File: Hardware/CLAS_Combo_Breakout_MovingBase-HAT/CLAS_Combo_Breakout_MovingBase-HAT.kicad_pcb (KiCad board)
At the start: 4 copper layers, 38.5 x 60 mm, 10 parts, among them J2 ZED, J3 NEO

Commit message: カイロズカッコカリ
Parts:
- added REF**: Converter_DCDC_AnalogDevices_LTM4693, Converter_DCDC_extlib:Converter_DCDC_AnalogDevices_LTM4693, F.Cu at (136.9, 100.7)
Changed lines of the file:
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@@
   (net 15 "/EXTINT_NEO")
   (net 16 "/RXD1_NEO")
+  (footprint "Converter_DCDC_extlib:Converter_DCDC_AnalogDevices_LTM4693" (layer "F.Cu")
+    (at 136.858 100.696)
+    (tags "LTM4693")
+    (attr smd)
+    (fp_text reference "REF**" (at 0 -3.175 unlocked) (layer "F.SilkS")
+      (effects (font (size 1 1) (thickness 0.15)))
+    )
+    (fp_text value "Converter_DCDC_AnalogDevices_LTM4693" (at 0 3.175 unlocked) (layer "F.Fab")
+      (effects (font (size 1 1) (thickness 0.15)))
+    )
+    (fp_text user "${REFERENCE}" (at 0 -3.175 unlocked) (layer "F.Fab")
+      (effects (font (size 1 1) (thickness 0.15)))
+    )
+    (fp_line (start 1.8796 -2.1209) (end -1.8796 -2.1209) (layer "F.SilkS") (width 0.12))
+    (fp_line (start 1.8796 2.1209) (end 1.8796 -2.1209) (layer "F.SilkS") (width 0.12))
+    (fp_line (start -1.3 -2.3609) (end -2.1196 -2.3609) (layer "F.SilkS") (width 0.12))
+    (fp_line (start -2.1196 -2.3609) (end -2.1196 -1.3) (layer "F.SilkS") (width 0.12))
+    (fp_line (start -1.8796 2.1209) (end 1.8796 2.1209) (layer "F.SilkS") (width 0.12))
+    (fp_line (start -1.8796 -2.1209) (end -1.8796 2.1209) (layer "F.SilkS") (width 0.12))
+    (fp_line (start 2.0066 -2.2479) (end 2.0066 2.2479) (layer "F.CrtYd") (width 0.05))
+    (fp_line (start -2.0066 -2.2479) (end 2.0066 -2.2479) (layer "F.CrtYd") (width 0.05))
+    (fp_line (start 2.0066 2.2479) (end -2.0066 2.2479) (layer "F.CrtYd") (width 0.05))
+    (fp_line (start -2.0066 2.2479) (end -2.0066 -2.2479) (layer "F.CrtYd") (width 0.05))
+    (fp_line (start 1.7526 -1.9939) (end -1.7526 -1.9939) (layer "F.Fab") (width 0.1))
+    (fp_line (start -1.4276 -1.9939) (end -1.7526 -1.6689) (layer "F.Fab") (width 0.1))
+    (fp_line (start 1.7526 1.9939) (end 1.7526 -1.9939) (layer "F.Fab") (width 0.1))
+    (fp_line (start -1.7526 1.9939) (end 1.7526 1.9939) (layer "F.Fab") (width 0.1))
+    (fp_line (start -1.7526 -1.9939) (end -1.7526 1.9939) (layer "F.Fab") (width 0.1))
+    (pad "A1" smd circle (at -1.3 -1.3) (size 0.45 0.45) (layers "F.Cu" "F.Paste" "F.Mask")
+      (solder_mask_margin -0.05) (solder_paste_margin -0.05))
+    (pad "A2" smd circle (at -0.65 -1.3) (size 0.45 0.45) (layers "F.Cu" "F.Paste" "F.Mask")
+      (solder_mask_margin -0.05) (solder_paste_margin -0.05))
+    (pad "A3" smd circle (at 0 -1.3) (size 0.45 0.45) (layers "F.Cu" "F.Paste" "F.Mask")
+      (solder_mask_margin -0.05) (solder_paste_margin -0.05))
+    (pad "A4" smd circle (at 0.65 -1.3) (size 0.45 0.45) (layers "F.Cu" "F.Paste" "F.Mask")
+      (solder_mask_margin -0.05) (solder_paste_margin -0.05))
+    (pad "A5" smd circle (at 1.3 -1.3) (size 0.45 0.45) (layers "F.Cu" "F.Paste" "F.Mask")
+      (solder_mask_margin -0.05) (solder_paste_margin -0.05))
+    (pad "B1" smd circle (at -1.3 -0.65) (size 0.45 0.45) (layers "F.Cu" "F.Paste" "F.Mask")
+      (solder_mask_margin -0.05) (solder_paste_margin -0.05))
+    (pad "B2" smd circle (at -0.65 -0.65) (size 0.45 0.45) (layers "F.Cu" "F.Paste" "F.Mask")
+      (solder_mask_margin -0.05) (solder_paste_margin -0.05))
+    (pad "B3" smd circle (at 0 -0.65) (size 0.45 0.45) (layers "F.Cu" "F.Paste" "F.Mask")
+      (solder_mask_margin -0.05) (solder_paste_margin -0.05))
+    (pad "B4" smd circle (at 0.65 -0.65) (size 0.45 0.45) (layers "F.Cu" "F.Paste" "F.Mask")
+      (solder_mask_margin -0.05) (solder_paste_margin -0.05))
+    (pad "B5" smd circle (at 1.3 -0.65) (size 0.45 0.45) (layers "F.Cu" "F.Paste" "F.Mask")
+      (solder_mask_margin -0.05) (solder_paste_margin -0.05))
+    (pad "C1" smd circle (at -1.3 0) (size 0.45 0.45) (layers "F.Cu" "F.Paste" "F.Mask")
+      (solder_mask_margin -0.05) (solder_paste_margin -0.05))
+    (pad "C2" smd circle (at -0.65 0) (size 0.45 0.45) (layers "F.Cu" "F.Paste" "F.Mask")
+      (solder_mask_margin -0.05) (solder_paste_margin -0.05))
+    (pad "C3" smd circle (at 0 0) (size 0.45 0.45) (layers "F.Cu" "F.Paste" "F.Mask")
+      (solder_mask_margin -0.05) (solder_paste_margin -0.05))
+    (pad "C4" smd circle (at 0.65 0) (size 0.45 0.45) (layers "F.Cu" "F.Paste" "F.Mask")
+      (solder_mask_margin -0.05) (solder_paste_margin -0.05))
+    (pad "C5" smd circle (at 1.3 0) (size 0.45 0.45) (layers "F.Cu" "F.Paste" "F.Mask")
+      (solder_mask_margin -0.05) (solder_paste_margin -0.05))
+    (pad "D1" smd circle (at -1.3 0.65) (size 0.45 0.45) (layers "F.Cu" "F.Paste" "F.Mask")
+      (solder_mask_margin -0.05) (solder_paste_margin -0.05))
+    (pad "D2" smd circle (at -0.65 0.65) (size 0.45 0.45) (layers "F.Cu" "F.Paste" "F.Mask")
+      (solder_mask_margin -0.05) (solder_paste_margin -0.05))
+    (pad "D3" smd circle (at 0 0.65) (size 0.45 0.45) (layers "F.Cu" "F.Paste" "F.Mask")
+      (solder_mask_margin -0.05) (solder_paste_margin -0.05))
+    (pad "D4" smd circle (at 0.65 0.65) (size 0.45 0.45) (layers "F.Cu" "F.Paste" "F.Mask")
+      (solder_mask_margin -0.05) (solder_paste_margin -0.05))
+    (pad "D5" smd circle (at 1.3 0.65) (size 0.45 0.45) (layers "F.Cu" "F.Paste" "F.Mask")
+      (solder_mask_margin -0.05) (solder_paste_margin -0.05))
+    (pad "E1" smd circle (at -1.3 1.3) (size 0.45 0.45) (layers "F.Cu" "F.Paste" "F.Mask")
+      (solder_mask_margin -0.05) (solder_paste_margin -0.05))
+    (pad "E2" smd circle (at -0.65 1.3) (size 0.45 0.45) (layers "F.Cu" "F.Paste" "F.Mask")
+      (solder_mask_margin -0.05) (solder_paste_margin -0.05))
+    (pad "E3" smd circle (at 0 1.3) (size 0.45 0.45) (layers "F.Cu" "F.Paste" "F.Mask")
+      (solder_mask_margin -0.05) (solder_paste_margin -0.05))
+    (pad "E4" smd circle (at 0.65 1.3) (size 0.45 0.45) (layers "F.Cu" "F.Paste" "F.Mask")
+      (solder_mask_margin -0.05) (solder_paste_margin -0.05))
+    (pad "E5" smd circle (at 1.3 1.3) (size 0.45 0.45) (layers "F.Cu" "F.Paste" "F.Mask")
+      (solder_mask_margin -0.05) (solder_paste_margin -0.05))
+    (model "${KIPRJMOD}/../../ExternalLib/Converter_DCDC_extlib/LTM4693.stp"
+      (offset (xyz 0 0 0))
+      (scale (xyz 1 1 1))
+      (rotate (xyz 0 0 0))
+    )
+  )
   (footprint "Connector_PinHeader_2.54mm:PinHeader_1x11_P2.54mm_Vertical" locked (layer "F.Cu")
     (at 127.94 147.912 90)

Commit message: 配線４割
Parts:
- removed the REF** at (136.9, 100.7)
- removed the REF** at (159.0, 96.0)
- removed the REF** at (160.0, 140.0)
- added C1: 0.1u, Capacitor_SMD:C_0603_1608Metric, F.Cu at (138.1, 122.0)
- added C10: 100μF10V X5R 3216, Capacitor_SMD:C_1206_3216Metric, F.Cu at (146.8, 138.8)
- added C11: 2200pF50V CH 1608, Capacitor_SMD:C_0603_1608Metric, F.Cu at (142.7, 145.4)
- added C12: 220μF4V X6S 3216, Capacitor_SMD:C_1206_3216Metric, F.Cu at (146.8, 144.9)
- added C2: 0.1u, Capacitor_SMD:C_0603_1608Metric, F.Cu at (133.0, 126.1)
- added C3: 0.1u, Capacitor_SMD:C_0603_1608Metric, F.Cu at (138.6, 156.6)
- added C4: 1u, Capacitor_SMD:C_0603_1608Metric, F.Cu at (140.7, 127.1)
- added C5: 0.1u, Capacitor_SMD:C_0603_1608Metric, F.Cu at (140.7, 125.6)
- added C6: 0.1u, Capacitor_SMD:C_0603_1608Metric, F.Cu at (138.1, 119.0)
- added C7: 47μF6.3V X5R 1608, Capacitor_SMD:C_0603_1608Metric, F.Cu at (143.2, 114.4)
- added C8: 0.1u, Capacitor_SMD:C_0603_1608Metric, F.Cu at (148.3, 132.7)
- added C9: 47μF6.3V X5R 1608, Capacitor_SMD:C_0603_1608Metric, F.Cu at (142.2, 132.7)
- added D1: CUHS20S30, CUHS20S30:CUHS20S30, F.Cu at (141.2, 118.0)
- added D2: RED, LED_SMD:LED_0603_1608Metric, F.Cu at (148.3, 129.7)
- added D3: GREEN, LED_SMD:LED_0603_1608Metric, F.Cu at (142.2, 129.7)
- added D4: RTK, LED_SMD:LED_0603_1608Metric, F.Cu at (130.5, 154.5)
- added D5: GEO, LED_SMD:LED_0603_1608Metric, F.Cu at (130.5, 157.1)
- added D6: PPS, LED_SMD:LED_0603_1608Metric, F.Cu at (130.5, 159.6)
- added D7: CUHS20S30, CUHS20S30:CUHS20S30, F.Cu at (145.2, 135.7)
- added J2: SMA, Connector_Coaxial_extlib:SMA_Molex_0732512440_embed, B.Cu at (148.5, 97.5)
- added J3: SWD, Connector_PinHeader_1.27mm:PinHeader_2x05_P1.27mm_Vertical, F.Cu at (138.1, 104.3)
- added J5: BATT, Connector_JST:JST_PH_S2B-PH-SM4-TB_1x02-1MP_P2.00mm_Horizontal, F.Cu at (136.3, 134.2)
- added J7: USB_C_Receptacle_USB2.0, Connector_USB_extlib:USB_C_Receptacle_5077CR-16-SMC2-BK-TR, F.Cu at (144.7, 108.3)
- added Q1: AO3415A, Package_TO_SOT_SMD:SOT-23, F.Cu at (142.7, 136.3)
- added R1: 33, Resistor_SMD:R_0603_1608Metric, F.Cu at (141.2, 122.0)
- added R10: 1M, Resistor_SMD:R_0603_1608Metric, F.Cu at (140.7, 130.9)
- added R11: 510k, Resistor_SMD:R_0603_1608Metric, F.Cu at (139.9, 128.6)
- added R12: 100k, Resistor_SMD:R_0603_1608Metric, F.Cu at (148.3, 135.7)
- added R13: 10, Resistor_SMD:R_0603_1608Metric, F.Cu at (146.8, 135.7)
- added R14: Rtop, Resistor_SMD:R_0603_1608Metric, F.Cu at (142.7, 139.3)
- added R15: Rbtm, Resistor_SMD:R_0603_1608Metric, F.Cu at (142.7, 140.8)
- added R16: 5.1k, Resistor_SMD:R_0603_1608Metric, F.Cu at (146.3, 102.7)
- added R17: 5.1k, Resistor_SMD:R_0603_1608Metric, F.Cu at (143.2, 102.7)
- added R18: 10k, Resistor_SMD:R_0603_1608Metric, F.Cu at (142.7, 143.9)
- added R19: 26.2k, Resistor_SMD:R_0603_1608Metric, F.Cu at (142.7, 142.4)
- added R2: 33, Resistor_SMD:R_0603_1608Metric, F.Cu at (134.6, 126.1)
- added R3: 10k, Resistor_SMD:R_0603_1608Metric, F.Cu at (139.7, 119.0)
- added R4: RILIM, Resistor_SMD:R_0603_1608Metric, F.Cu at (145.2, 129.7)
- added R5: 1k, Resistor_SMD:R_0603_1608Metric, F.Cu at (146.8, 129.7)
- added R6: 1k, Resistor_SMD:R_0603_1608Metric, F.Cu at (143.7, 129.7)
- added R7: 1k, Resistor_SMD:R_0603_1608Metric, F.Cu at (134.1, 154.5)
- added R8: 1k, Resistor_SMD:R_0603_1608Metric, F.Cu at (134.1, 157.1)
- added R9: 1k, Resistor_SMD:R_0603_1608Metric, F.Cu at (134.1, 159.6)
- added REF**: LiPo_3.7V_500mAh_503030, Battery_extlib:LiPo_3.7V_500mAh_503030, B.Cu at (145.0, 130.0)
- added SW1: SW_Push, Button_Switch_SMD:SW_Push_1P1T_NO_Vertical_Wuerth_434133025816, F.Cu at (134.6, 115.9)
- added SW2: SW_SPDT, Button_Switch_SMD_extlib:SW_SPDT_SSSS213202, F.Cu at (136.6, 142.4)
- added U1: CH340K, Package_SO:SSOP-10_3.9x4.9mm_P1.00mm, F.Cu at (134.6, 121.0)
- added U2: TMUX136, Package_DFN_QFN:Texas_R-PUQFN-N10, F.Cu at (136.6, 126.1)
- added U3: ISP4520-AS, RF_Module_extlib:ISP4520-AS_with_Keep-Out, F.Cu at (159.5, 115.5)
- added U4: MCP73831-2-OT, Package_TO_SOT_SMD:SOT-23-5, F.Cu at (145.2, 132.7)
- added U5: LTM4693, Converter_DCDC_extlib:Converter_DCDC_AnalogDevices_LTM4693, F.Cu at (146.8, 141.8)
- added U6: USBLC6-2P6, Package_TO_SOT_SMD:SOT-666, F.Cu at (139.7, 112.9)
- J1: renamed from J**; value 0734152063 -> MMCX
- moved H4 66.9 mm to (144.0, 158.0)
- renumbered J2 to J4, J3 to J6
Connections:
- J1 pad 1: (no net) -> Net-(J1-Pad1)
- J1 pad 2: (no net) -> GND
- J6 pad 2: /RESET -> /RESET_ZED_NEO
- J6 pad 8: /SDA -> unconnected-(J6-Pad8)
- J6 pad 9: /SCL -> unconnected-(J6-Pad9)
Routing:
- net Net-(R15-Pad1): track 0.00 -> 15.8 mm
- net VBUS: track 0.00 -> 10.5 mm
- net +BATT: track 0.00 -> 9.61 mm
- net VDD: track 0.00 -> 8.55 mm
- net Net-(Q1-Pad1): track 0.00 -> 7.82 mm, vias 0 -> 2
- net Net-(R14-Pad2): track 0.00 -> 7.52 mm
- net /~{CHG_STAT}: track 0.00 -> 5.39 mm
- net +3.3V: track 0.00 -> 3.39 mm
- net Net-(R18-Pad1): track 0.00 -> 2.24 mm
- net Net-(R4-Pad2): track 0.00 -> 2.20 mm
- net Net-(R19-Pad1): track 0.00 -> 2.00 mm
- net Net-(C11-Pad1): track 0.00 -> 1.54 mm
- net Net-(D3-Pad2): track 0.00 -> 1.54 mm
- net Net-(D2-Pad1): track 0.00 -> 1.54 mm
- net /VBAT: track 0.00 -> 1.49 mm
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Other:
- outline, holes or cut-outs redrawn
- board text added: "CHG"
- board text added: "FULL"
- board text added: "ISP4520のy位置はkeep-outエリアの下側が 右下MHのすぐ上にくるように配置"
- board text added: "PROG"
- board text added: "SMAコネクタのサーマルリリーフ消す"
- board text added: "SMAコネクタは下のボードのUSBコネクタに干渉しない位置 なおType-Cケーブルを接続する場合については未確認"
- board text added: "左側の基板エッジは左上のMHに従属"

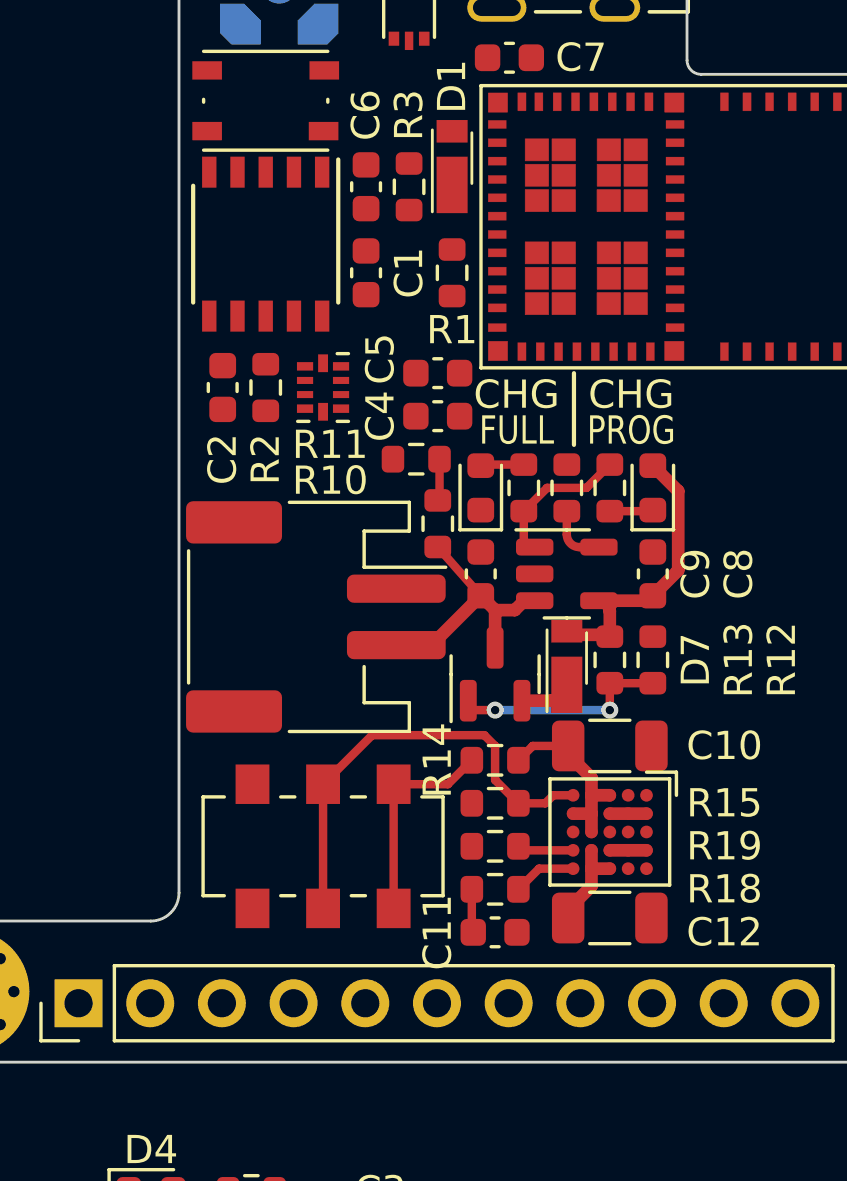
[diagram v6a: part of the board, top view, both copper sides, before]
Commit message: ISP4520の公式のフットプリントの間違いを修正
メーカーが提供しているフットプリントでも信用しないようにしましょう
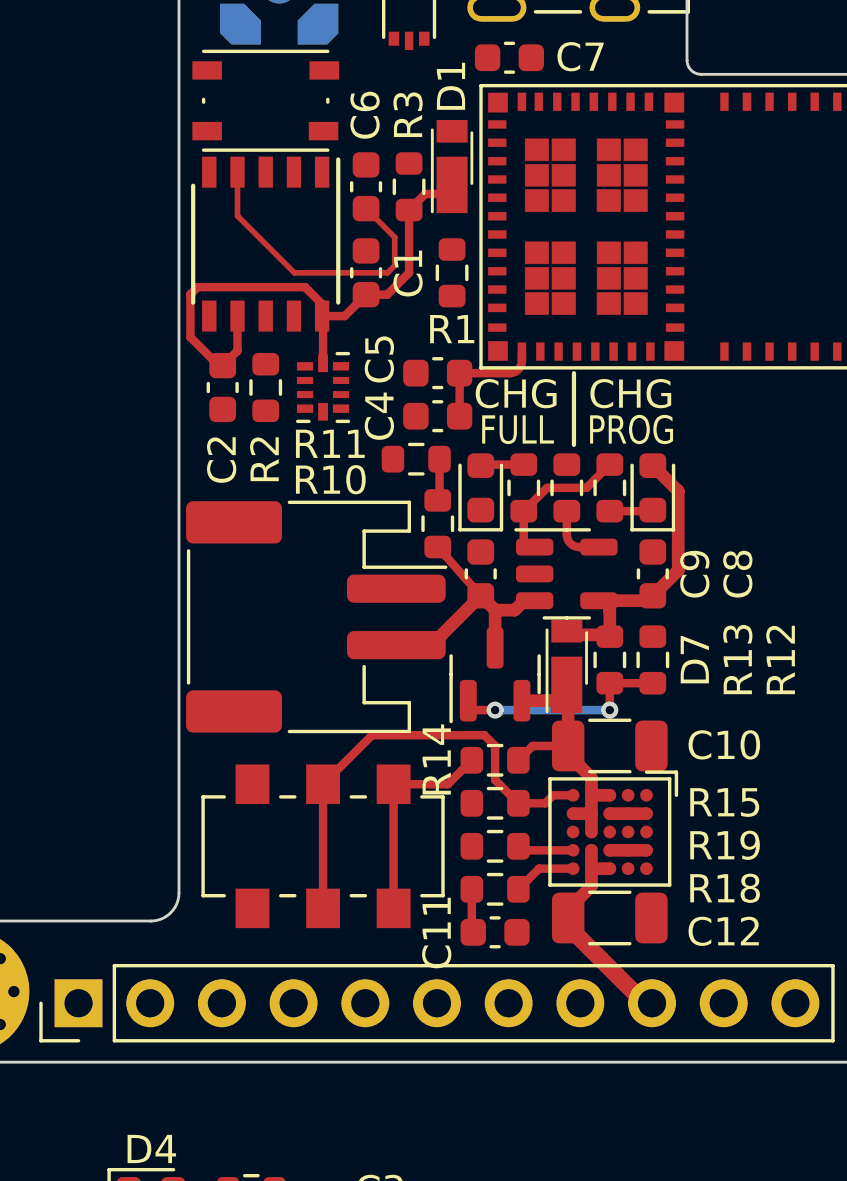
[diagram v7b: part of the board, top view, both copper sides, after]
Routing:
- net +3.3V: track 3.39 -> 32.3 mm
- net /DTR: track 0.00 -> 10.5 mm
- net VDD: track 8.55 -> 10.7 mm
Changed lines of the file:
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@@
     (effects (font (size 1 1) (thickness 0.15)) (justify left))
   )
+  (segment (start 141.443 125.588) (end 141.443 127.112) (width 0.3) (layer "F.Cu") (net 2))
+  (segment (start 137.369 123.566) (end 138.128 122.807) (width 0.3) (layer "F.Cu") (net 2))
+  (segment (start 138.877 122.807) (end 138.128 122.807) (width 0.3) (layer "F.Cu") (net 2))
+  (segment (start 131.905 124.318) (end 131.905 122.794) (width 0.3) (layer "F.Cu") (net 2))
   (segment (start 146.114 142.494) (end 146.114 143.144) (width 0.45) (layer "F.Cu") (net 2))
+  (segment (start 132.908 125.321) (end 131.905 124.318) (width 0.3) (layer "F.Cu") (net 2))
+  (segment (start 139.652 119.809) (end 139.652 122.032) (width 0.3) (layer "F.Cu") (net 2))
+  (segment (start 132.159 122.54) (end 135.969 122.54) (width 0.3) (layer "F.Cu") (net 2))
+  (segment (start 141.176 118.918) (end 141.176 119.238) (width 0.3) (layer "F.Cu") (net 2))
   (segment (start 145.289 144.589) (end 145.289 144.892) (width 0.45) (layer "F.Cu") (net 2))
+  (segment (start 145.289 144.892) (end 145.289 145.195) (width 0.6) (layer "F.Cu") (net 2))
+  (segment (start 136.572 123.566) (end 137.369 123.566) (width 0.3) (layer "F.Cu") (net 2))
+  (segment (start 139.652 122.032) (end 138.877 122.807) (width 0.3) (layer "F.Cu") (net 2))
+  (segment (start 131.905 122.794) (end 132.159 122.54) (width 0.3) (layer "F.Cu") (net 2))
+  (segment (start 135.969 122.54) (end 136.572 123.143) (width 0.3) (layer "F.Cu") (net 2))
+  (segment (start 133.572 124.797) (end 133.048 125.321) (width 0.3) (layer "F.Cu") (net 2))
   (segment (start 146.114 143.764) (end 145.289 144.589) (width 0.45) (layer "F.Cu") (net 2))
+  (segment (start 133.048 125.321) (end 132.908 125.321) (width 0.3) (layer "F.Cu") (net 2))
+  (segment (start 148.006 147.912) (end 148.26 147.912) (width 0.6) (layer "F.Cu") (net 2))
+  (segment (start 145.289 145.195) (end 148.006 147.912) (width 0.6) (layer "F.Cu") (net 2))
+  (segment (start 143.65 124.825) (end 143.65 125.146) (width 0.3) (layer "F.Cu") (net 2))
+  (segment (start 136.572 123.143) (end 136.572 123.566) (width 0.3) (layer "F.Cu") (net 2))
+  (segment (start 141.176 119.238) (end 140.223 119.238) (width 0.3) (layer "F.Cu") (net 2))
+  (segment (start 133.572 123.566) (end 133.572 124.797) (width 0.3) (layer "F.Cu") (net 2))
   (segment (start 146.114 143.144) (end 146.114 143.764) (width 0.45) (layer "F.Cu") (net 2))
+  (segment (start 136.604 123.598) (end 136.572 123.566) (width 0.3) (layer "F.Cu") (net 2))
   (segment (start 146.114 143.144) (end 146.764 143.144) (width 0.45) (layer "F.Cu") (net 2))
+  (segment (start 140.223 119.238) (end 139.652 119.809) (width 0.3) (layer "F.Cu") (net 2))
+  (segment (start 136.604 125.236) (end 136.604 123.598) (width 0.3) (layer "F.Cu") (net 2))
+  (segment (start 143.208 125.588) (end 141.443 125.588) (width 0.3) (layer "F.Cu") (net 2))
+  (arc (start 143.65 125.146) (mid 143.520541 125.458541) (end 143.208 125.588) (width 0.3) (layer "F.Cu") (net 2))
+  (segment (start 139.144 121.778) (end 138.89 122.032) (width 0.2) (layer "F.Cu") (net 17))
+  (segment (start 139.144 120.775) (end 139.144 121.778) (width 0.2) (layer "F.Cu") (net 17))
+  (segment (start 138.128 119.759) (end 139.144 120.775) (width 0.2) (layer "F.Cu") (net 17))
+  (segment (start 135.588 122.032) (end 133.572 120.016) (width 0.2) (layer "F.Cu") (net 17))
+  (segment (start 133.572 120.016) (end 133.572 118.466) (width 0.2) (layer "F.Cu") (net 17))
+  (segment (start 138.89 122.032) (end 135.588 122.032) (width 0.2) (layer "F.Cu") (net 17))
   (segment (start 149.188 129.7645) (end 148.288 128.8645) (width 0.45) (layer "F.Cu") (net 18))
   (segment (start 146.764 134.923) (end 146.764 134.0365) (width 0.45) (layer "F.Cu") (net 18))
@@
   (segment (start 145.289 138.796) (end 144.033 138.796) (width 0.3) (layer "F.Cu") (net 20))
   (segment (start 146.764 140.544) (end 146.114 140.544) (width 0.45) (layer "F.Cu") (net 20))
+  (segment (start 145.289 136.681) (end 145.24 136.632) (width 0.45) (layer "F.Cu") (net 20))
   (segment (start 145.289 139.099) (end 145.289 138.796) (width 0.45) (layer "F.Cu") (net 20))
+  (segment (start 145.289 138.796) (end 145.289 136.681) (width 0.45) (layer "F.Cu") (net 20))
   (segment (start 146.114 139.924) (end 145.289 139.099) (width 0.45) (layer "F.Cu") (net 20))
   (segment (start 146.114 140.544) (end 146.114 139.924) (width 0.45) (layer "F.Cu") (net 20))
